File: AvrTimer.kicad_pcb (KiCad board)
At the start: 2 copper layers, 40 parts, among them Q1 BC846, Q10 BC557, Q11 BC557, Q12 BC557, Q2 BC846, Q3 BC846, Q4 BC846, Q5 BC846, Q6 BC846, Q7 BC846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

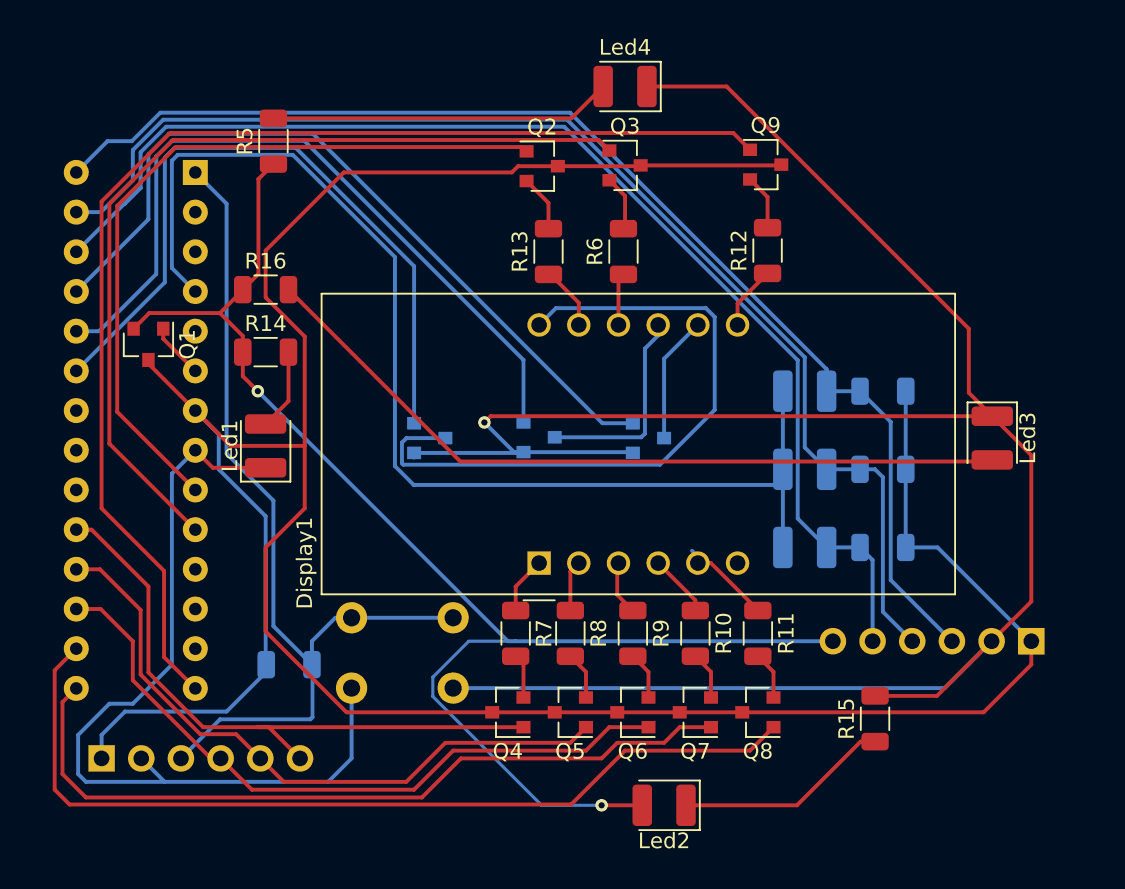
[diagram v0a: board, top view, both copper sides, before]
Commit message: Partly update scheme for hand-soldering
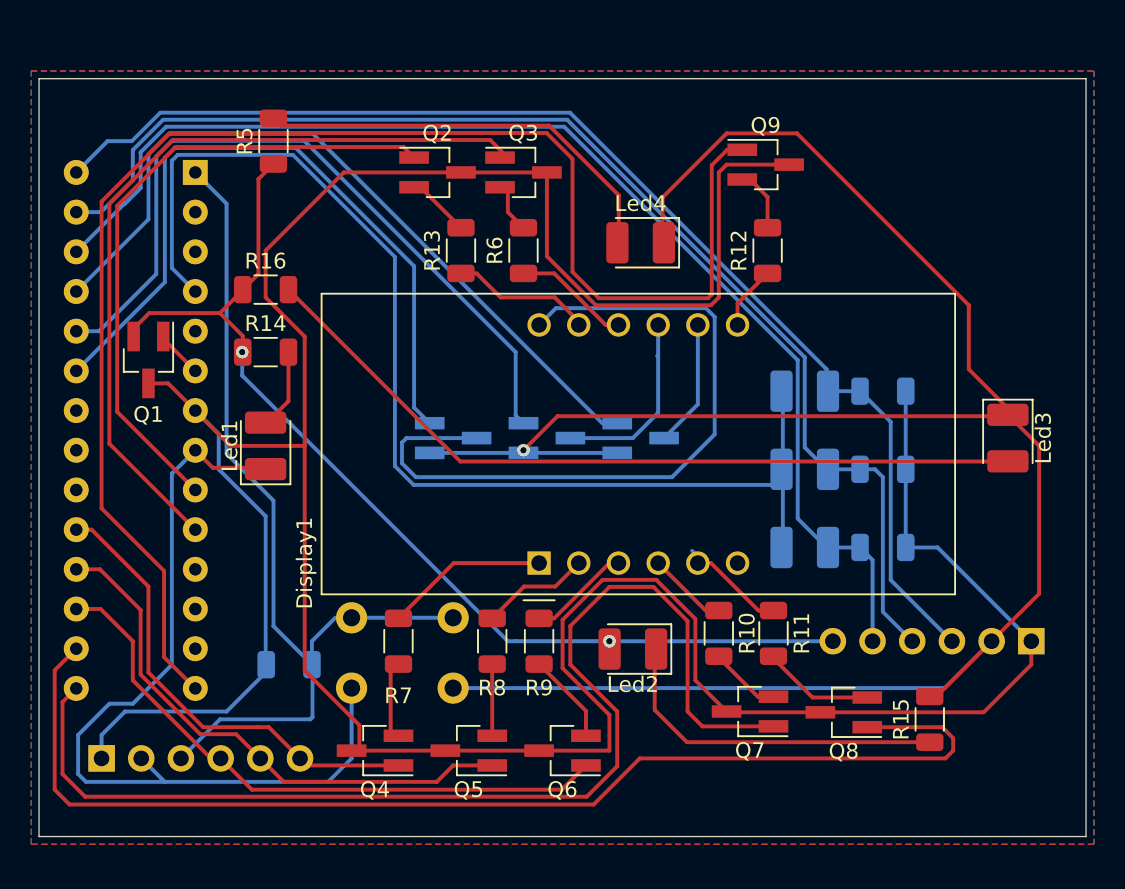
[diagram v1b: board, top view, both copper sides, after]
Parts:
- D4, D5, D6: footprint Diode_SMD:D_1210_3225Metric -> Diode_SMD:D_1210_3225Metric_Pad1.42x2.65mm_HandSolder
- Led1, Led2, Led3: footprint LED_SMD:LED_1210_3225Metric -> LED_SMD:LED_1210_3225Metric_Pad1.42x2.65mm_HandSolder
- Led4: footprint Diode_SMD:D_1210_3225Metric -> LED_SMD:LED_1210_3225Metric_Pad1.42x2.65mm_HandSolder
- Q1, Q10, Q11, Q12, Q2, Q3, Q4, Q5, Q6, Q7, Q8, Q9: footprint Package_TO_SOT_SMD:SOT-23 -> Package_TO_SOT_SMD:SOT-23_Handsoldering
- moved Led2 10.2 mm to (116.0, 85.5)
- moved Led4 10.0 mm to (116.5, 59.5)
- moved Q4 8.85 mm to (99.5, 92.0)
- moved R7 7.52 mm to (101.0, 85.0)
- moved Q5 6.95 mm to (105.5, 92.0)
- moved Q2 6.71 mm to (103.5, 55.0)
- moved Q3 6.52 mm to (109.0, 55.0)
- moved R6 6.40 mm to (109.0, 60.0)
- moved R9 6.02 mm to (110.0, 85.0)
- moved R13 5.60 mm to (105.0, 60.0)
- moved Q8 5.50 mm to (129.5, 89.5)
- moved Q6 5.12 mm to (111.5, 92.0)
- moved R8 5.02 mm to (107.0, 85.0)
- moved Q7 3.50 mm to (123.5, 89.5)
- moved R15 3.50 mm to (135.0, 90.0)
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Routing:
- net VCC: track 180.9 -> 213.5 mm
- net Net-(Controller1-Pad15): track 49.8 -> 74.1 mm
- net Net-(Controller1-Pad14): track 77.4 -> 94.9 mm
- net Net-(Controller1-Pad16): track 58.0 -> 75.5 mm
- net Net-(Led2-Pad2): track 90.1 -> 72.9 mm
- net Net-(Controller1-Pad19): track 40.6 -> 29.6 mm
- net Net-(Led2-Pad1): track 13.8 -> 22.4 mm
- net Net-(Controller1-Pad9): track 48.1 -> 41.1 mm
- net Net-(Controller1-Pad18): track 42.1 -> 35.1 mm
- net Net-(Display1-Pad1): track 3.66 -> 10.5 mm
- net Net-(Controller1-Pad10): track 57.1 -> 50.8 mm
- net GND: track 199.3 -> 193.3 mm
- net Net-(Led4-Pad2): track 21.9 -> 27.2 mm
- net Net-(Controller1-Pad17): track 44.5 -> 39.5 mm
- net Net-(Display1-Pad11): track 4.16 -> 9.03 mm
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- added copper zone on B.Cu, net GND
- added copper zone on F.Cu, net GND
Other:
- board outline added: 67 x 48.5 mm

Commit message: Update all footprints to correct ones
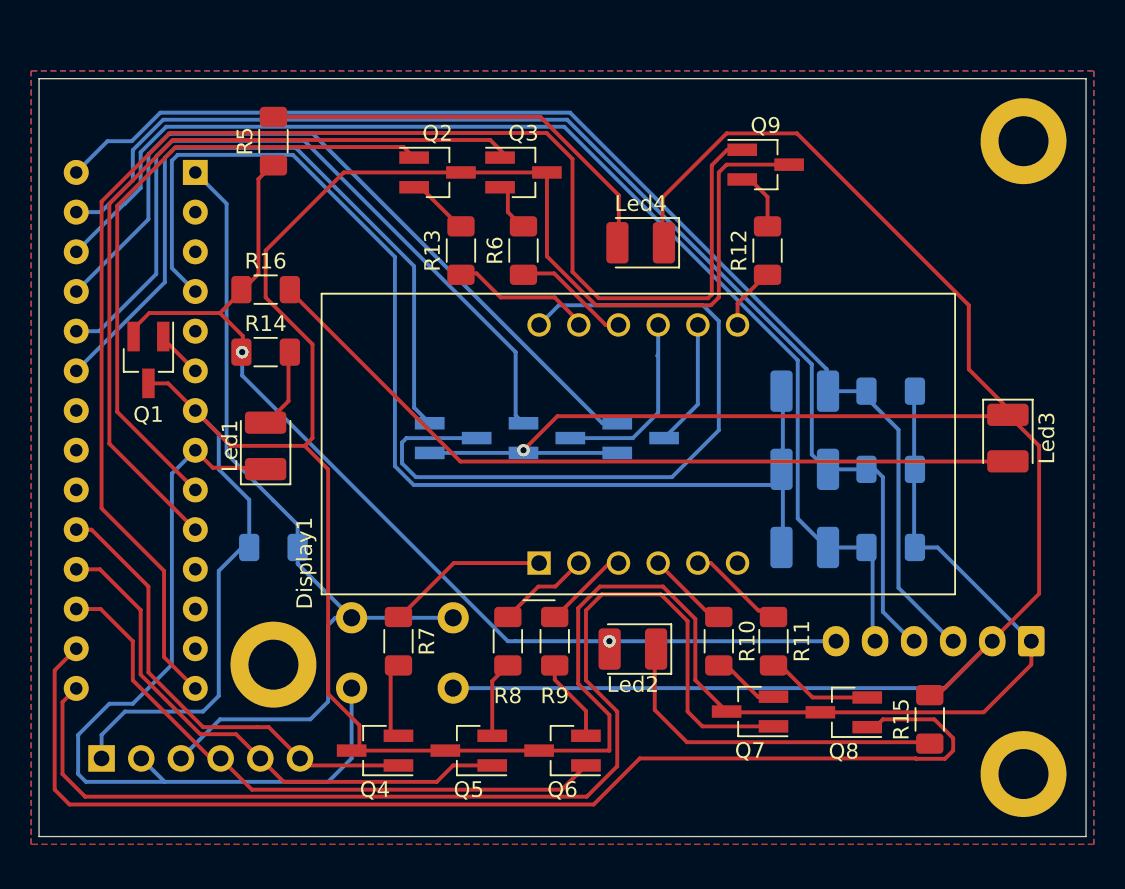
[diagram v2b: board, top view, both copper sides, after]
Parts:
- added ?: , , F.Cu at (141.0, 93.5)
- added ?: , , F.Cu at (93.0, 86.5)
- added ?: , , F.Cu at (141.0, 53.0)
- Mechanic1: footprint Connector_PinSocket_2.54mm:PinSocket_1x06_P2.54mm_Vertical -> Connector_JST:JST_XH_B6B-XH-A_1x06_P2.50mm_Vertical
- R1, R10, R11, R12, R13, R14, R15, R16, R2, R3, R4, R5, R6, R7, R8, R9: footprint Resistor_SMD:R_1206_3216Metric -> Resistor_SMD:R_1206_3216Metric_Pad1.30x1.75mm_HandSolder
- Serial1: footprint Connector_PinSocket_2.54mm:PinSocket_1x06_P2.54mm_Vertical -> Connector_PinHeader_2.54mm:PinHeader_1x06_P2.54mm_Vertical
- moved R4 7.57 mm to (93.0, 79.0)
- moved R8 1.00 mm to (108.0, 85.0)
- moved R9 1.00 mm to (111.0, 85.0)
- moved R1 0.50 mm to (132.5, 69.0)
- moved R10 0.50 mm to (121.5, 85.0)
- moved R11 0.50 mm to (125.0, 85.0)
- moved R2 0.50 mm to (132.5, 74.0)
- moved R3 0.50 mm to (132.5, 79.0)
- turned Mechanic1 to 180 degrees
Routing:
- net VCC: track 213.5 -> 210.5 mm
- net Net-(Controller1-Pad1): track 58.6 -> 56.7 mm
- net Net-(Controller1-Pad15): track 74.1 -> 72.9 mm
- net Net-(Display1-Pad2): track 7.01 -> 5.97 mm
- net Net-(Display1-Pad3): track 7.20 -> 6.16 mm
- net Net-(Q6-Pad2): track 6.33 -> 5.83 mm

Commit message: Update after Alexander's Y. review
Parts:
- moved R16 49.9 mm to (139.9, 78.0), turned to 90 degrees
- moved R5 23.6 mm to (116.5, 56.0), turned to 0 degrees
- moved Q1 8.99 mm to (92.5, 62.0), turned to 180 degrees
- moved Q10 5.02 mm to (115.5, 71.5), turned to 90 degrees
- moved Q12 5.02 mm to (109.5, 71.5), turned to 90 degrees
- moved Q11 4.53 mm to (121.0, 71.5), turned to 90 degrees
- moved Q8 4.25 mm to (125.5, 91.0), turned to -90 degrees
- moved Q7 3.35 mm to (120.5, 91.0), turned to -90 degrees
- moved R13 2.74 mm to (102.5, 61.0), turned to 180 degrees
- moved Q5 2.69 mm to (108.0, 91.0), turned to -90 degrees
- moved Q6 2.24 mm to (113.5, 91.0), turned to -90 degrees
- moved R1 1.58 mm to (133.0, 67.5)
- moved R15 1.58 mm to (133.5, 89.5), turned to 0 degrees
- moved R2 1.58 mm to (133.0, 72.5)
- moved R3 1.58 mm to (133.0, 77.5)
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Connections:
- Led2 pad 1: Net-(Led2-Pad1) -> GND
- Led2 pad 2: Net-(Led2-Pad2) -> Net-(R15-Pad2)
- Mechanic1 pad 6: Net-(Led2-Pad2) -> Net-(Mechanic1-Pad6)
- Q1 pad 2: Net-(Led2-Pad2) -> Net-(Mechanic1-Pad6)
- Q11 pad 2: Net-(Controller1-Pad25) -> Net-(Controller1-Pad23)
- Q12 pad 2: Net-(Controller1-Pad23) -> Net-(Controller1-Pad25)
- R14 pad 1: Net-(Led2-Pad2) -> Net-(Mechanic1-Pad6)
- R15 pad 1: Net-(Led2-Pad1) -> Net-(Mechanic1-Pad6)
- R15 pad 2: GND -> Net-(R15-Pad2)
- R16 pad 1: Net-(Led2-Pad2) -> Net-(Mechanic1-Pad6)
- R5 pad 1: Net-(Led2-Pad2) -> Net-(Mechanic1-Pad6)
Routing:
- net GND: track 193.3 -> 0.00 mm, vias 1 -> 30
- net Net-(Mechanic1-Pad6): track 0.00 -> 119.0 mm, vias 0 -> 4
- net Net-(Led2-Pad2): track 72.9 -> 0.00 mm, vias 2 -> 0
- net Net-(Led3-Pad2): track 50.6 -> 2.98 mm
- net Net-(Q12-Pad3): track 47.5 -> 6.15 mm
- net Net-(Controller1-Pad23): track 45.8 -> 78.2 mm
- net VCC: track 210.5 -> 181.5 mm
- net Net-(R15-Pad2): track 0.00 -> 24.5 mm, vias 0 -> 2
- net Net-(Led4-Pad2): track 27.3 -> 3.51 mm
- net Net-(Controller1-Pad28): track 78.4 -> 101.6 mm, vias 0 -> 2
- net Net-(Led2-Pad1): track 22.4 -> 0.00 mm
- net Net-(Controller1-Pad24): track 47.9 -> 70.2 mm
- net Net-(Controller1-Pad26): track 78.8 -> 99.0 mm, vias 0 -> 2
- net Net-(Controller1-Pad27): track 79.3 -> 98.8 mm, vias 0 -> 2
- net Net-(Controller1-Pad15): track 72.9 -> 57.0 mm, vias 0 -> 2
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
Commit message: Final version of base board
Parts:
- moved D4 1.00 mm to (127.0, 76.5)
- moved D5 1.00 mm to (127.0, 71.5)
- moved D6 1.00 mm to (127.0, 66.5)
- moved R1 1.00 mm to (133.0, 66.5)
- moved R2 1.00 mm to (133.0, 71.5)
- moved R3 1.00 mm to (133.0, 76.5)
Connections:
- Controller1 pad 20: unconnected-(Controller1-Pad20) -> VCC
- Controller1 pad 22: unconnected-(Controller1-Pad22) -> GND
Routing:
- net VCC: track 181.5 -> 188.2 mm
- net Net-(Controller1-Pad4): track 83.1 -> 81.9 mm
- net Net-(Controller1-Pad26): track 99.0 -> 100.0 mm
- net Net-(Controller1-Pad10): track 52.8 -> 53.6 mm
- net Net-(Controller1-Pad27): track 98.8 -> 99.4 mm
- net Net-(Controller1-Pad15): vias 2 -> 1
- net GND: vias 30 -> 37
